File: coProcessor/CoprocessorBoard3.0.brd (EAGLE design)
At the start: 101.6 x 101.6 mm, 76 parts, among them IC1 STM32F405RGT6

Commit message: (Hulk) Smash
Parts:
- added C1: (no value), rcl:E2-5
- moved GPIO_CONNECTOR 17.9 mm to (43.5, 26.1)
- moved OSC_C1 3.70 mm to (43.7, 37.0)
- moved DEBUG 3.38 mm to (31.5, 34.5), turned to 90 degrees
- moved OSC_C2 3.31 mm to (48.3, 37.1)
- moved OSCILLATOR 2.84 mm to (47.2, 33.0)
- moved POWER_JACK 1.42 mm to (5.16, 17.4)
- moved D+SERIES 0.63 mm to (33.3, 74.9)
- moved D-SERIES 0.61 mm to (36.2, 74.9)
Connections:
- net 3V3: now also C1.+
- net GND: now also C1.-
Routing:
- net PC14: track 8.27 -> 29.1 mm
- net 3V3: track 266.0 -> 286.4 mm
- net PC13: track 8.81 -> 27.9 mm
- net MISSION_START: track 58.7 -> 77.5 mm
- net SWITCH_3: track 59.7 -> 77.4 mm
- net SWITCH_4: track 60.3 -> 77.5 mm
- net SWITCH_5: track 61.2 -> 78.0 mm
- net PB8: track 15.6 -> 30.9 mm
- net GND: track 82.7 -> 89.1 mm, vias 13 -> 14
- net RCC_OSC_OUT: track 17.8 -> 19.6 mm
- net USB_OTG_HS_DM: track 10.6 -> 11.2 mm
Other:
- board text added: "3.3V"
- board text added: "JTDI"
- board text added: "PA4"
- board text added: "PA5"
- board text added: "PC4"
- board text added: "PC5"
- board text added: "PC6"
- board text added: "PC7"
- board text added: "SWDIO"

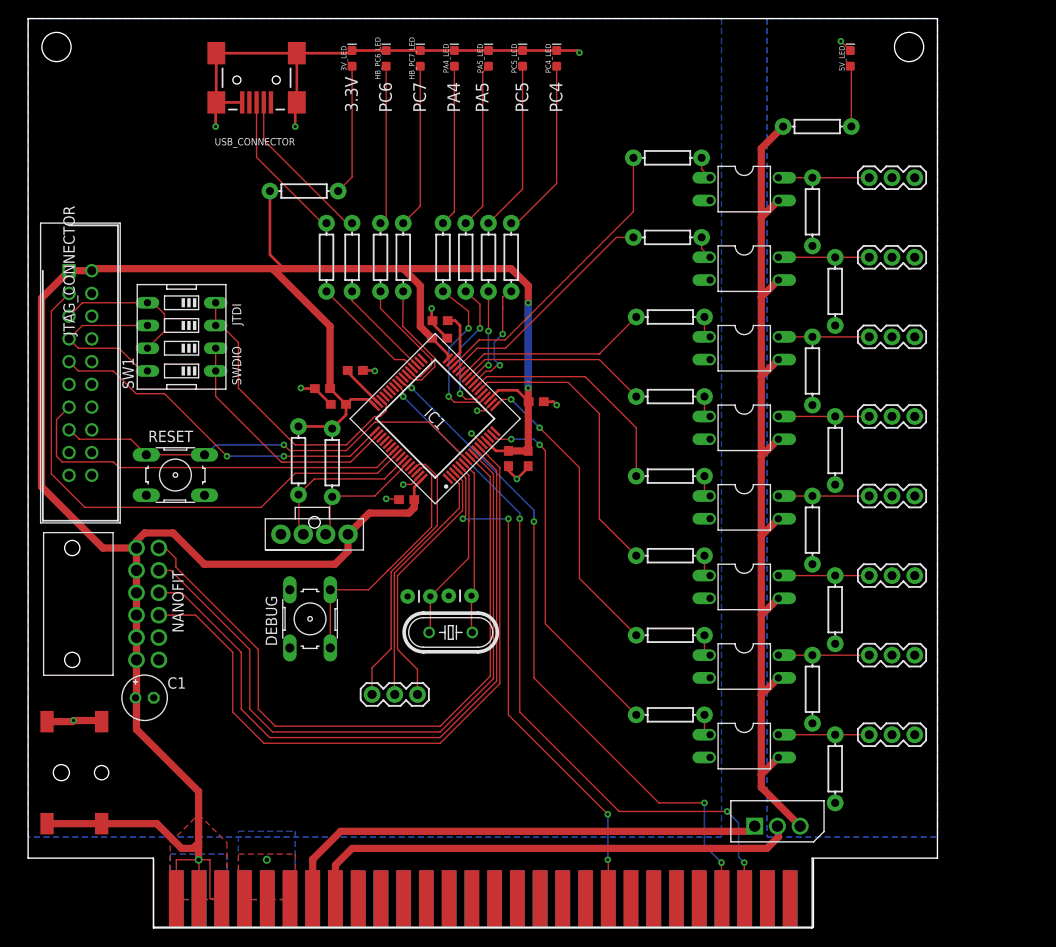
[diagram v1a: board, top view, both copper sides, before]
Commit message: Adding labels to everything
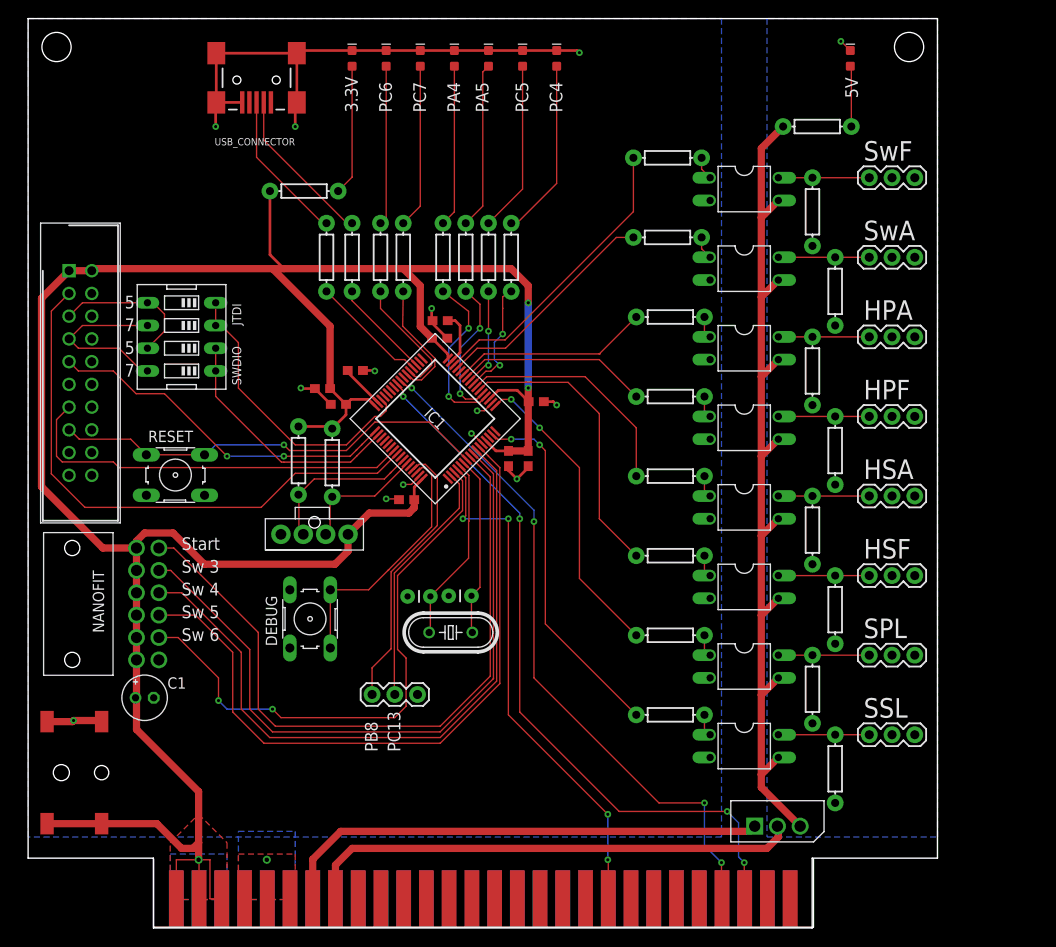
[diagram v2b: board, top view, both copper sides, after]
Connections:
- removed net PC14: GPIO_CONNECTOR.1, IC1.3
- new net SWITCH_6: IC1.3, SWITCH_CONNECTOR.CK2
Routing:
- net SWITCH_6: track 0.00 -> 63.3 mm, vias 0 -> 2
- net PC14: track 29.1 -> 0.00 mm
- net MISSION_START: track 77.5 -> 78.8 mm
- net RCC_OSC_OUT: track 19.6 -> 20.1 mm
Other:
- board text added: "5"
- board text added: "5V"
- board text added: "7"
- board text added: "HPA"
- board text added: "HPF"
- board text added: "HSA"
- board text added: "HSF"
- board text added: "PB8"
- board text added: "PC13"
- board text added: "SPL"
- board text added: "SSL"
- board text added: "Start"
- board text added: "Sw 3"
- board text added: "Sw 4"
- board text added: "Sw 5"
- board text added: "Sw 6"
- board text added: "SwA"
- board text added: "SwF"

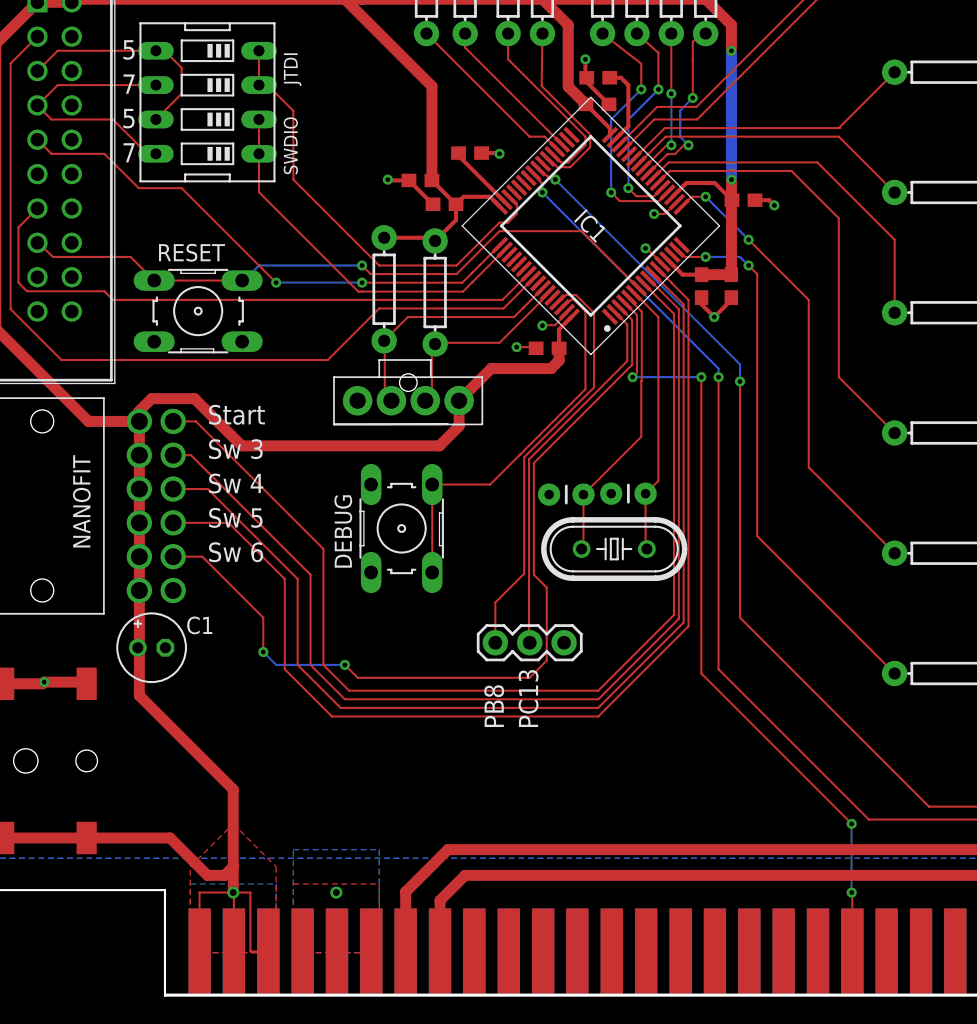
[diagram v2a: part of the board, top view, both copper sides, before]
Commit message: Added low pass filter, ran DRC fixed weird issue
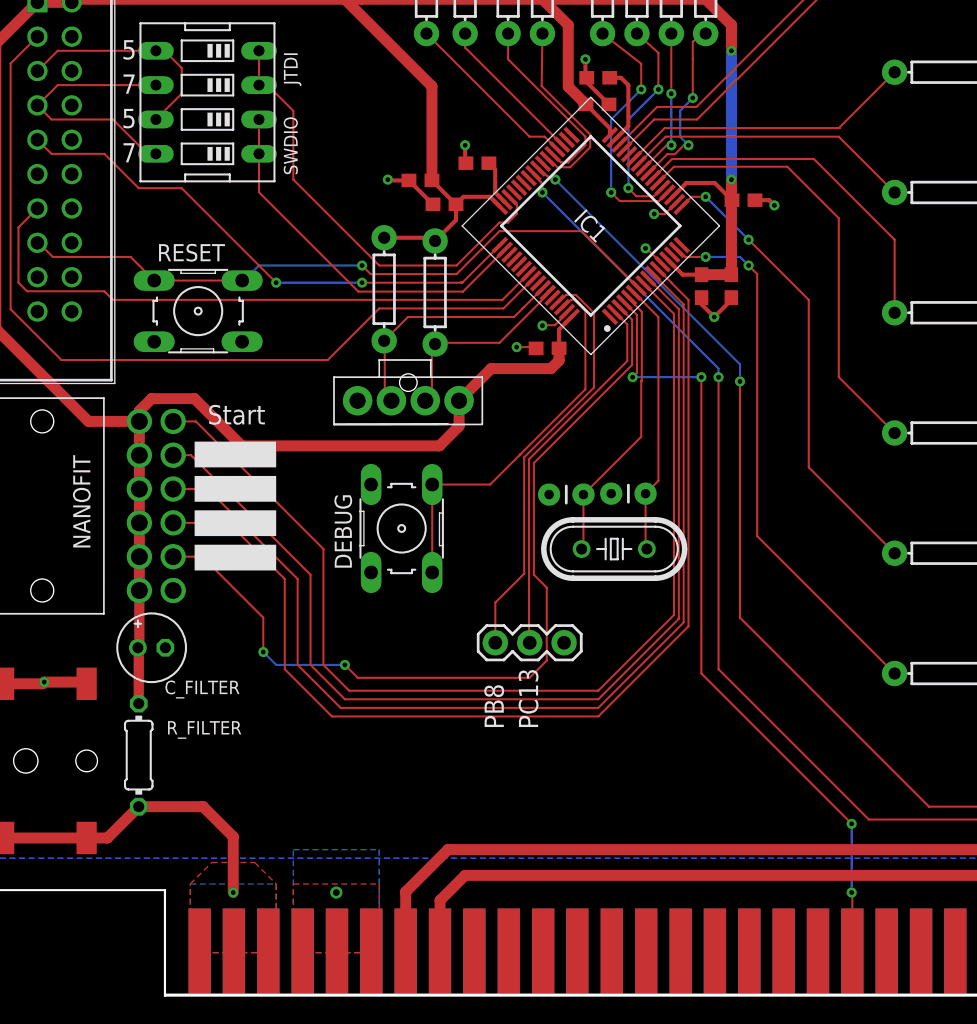
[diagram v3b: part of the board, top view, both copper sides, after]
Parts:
- added R_FILTER: (no value), rcl:0204/7
- moved CAP2 0.92 mm to (37.1, 61.5), turned to 180 degrees
- renumbered C1 to C_FILTER
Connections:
- new net 3V3_RAW: POWER_JACK.1.1, POWER_JACK.1.2, R_FILTER.1, U$1.3.3VP1, U$1.3.3VP2, U$1.3.3VP3, U$1.3.3V_4, U$1.3.3V_5, U$1.3.3V_6
- net 3V3: now also R_FILTER.2; no longer POWER_JACK.1.1, POWER_JACK.1.2, U$1.3.3VP1, U$1.3.3VP2, U$1.3.3VP3, U$1.3.3V_4, U$1.3.3V_5, U$1.3.3V_6
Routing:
- net 3V3: track 286.4 -> 233.0 mm, vias 3 -> 2
- net 3V3_RAW: track 0.00 -> 22.9 mm, vias 0 -> 1
- net VCAP2: track 5.03 -> 3.36 mm
- added copper zone on layer 1, net 3V3_RAW
- added copper zone on layer 16, net 3V3_RAW
- removed copper zone on layer 1, net 3V3
- removed copper zone on layer 16, net 3V3
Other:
- board text removed: "Sw 3"
- board text removed: "Sw 4"
- board text removed: "Sw 5"
- board text removed: "Sw 6"

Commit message: Merging to fix with the stuff
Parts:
- added ESC_CONNECTOR_1: 455-1750-1-ND, SparkFun-Connectors:1X03
- added OPTOCOUPLER_1: SFH610, optocoupler:DIL04
- added O_IN_1: 220, SparkFun-Resistors:AXIAL-0.3
- added O_R1: 10k, SparkFun-Resistors:AXIAL-0.3
- moved O_IN_2 9.23 mm to (65.7, 30.8)
- moved O_R2 7.31 mm to (90.5, 25.1)
- moved OPTOCOUPLER_2 7.23 mm to (80.0, 27.5)
- moved ESC_CONNECTOR_2 7.20 mm to (94.0, 28.8)
- moved O_IN_4 7.16 mm to (69.5, 39.5)
- moved OPTOCOUPLER_4 6.52 mm to (80.0, 35.7)
- moved ESC_CONNECTOR_4 6.49 mm to (94.0, 37.0)
- moved O_IN_5 6.49 mm to (69.5, 47.7)
- moved O_R4 6.30 mm to (87.6, 33.0)
- moved O_IN_6 5.83 mm to (69.5, 55.9)
- moved OPTOCOUPLER_5 5.80 mm to (80.0, 43.9)
- moved ESC_CONNECTOR_5 5.78 mm to (94.0, 45.1)
- moved O_R5 5.71 mm to (90.2, 41.3)
- moved O_R6 5.19 mm to (87.6, 49.6)
- moved O_IN_7 5.18 mm to (69.5, 64.0)
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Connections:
- new net N$1: ESC_CONNECTOR_1.1, OPTOCOUPLER_1.4, O_R1.P$1
- new net N$3: OPTOCOUPLER_1.1, O_IN_1.P$2
- net +5V: now also OPTOCOUPLER_1.3
- net GND: now also OPTOCOUPLER_1.2
- net GNDBAT: now also ESC_CONNECTOR_1.3, O_R1.P$2
- net SURGEPORTHI: now also O_IN_1.P$1
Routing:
- net SURGEPORTHI: track 0.00 -> 40.7 mm, vias 0 -> 2
- net N$1: track 0.00 -> 19.0 mm
- net SURGESTBDLOW: track 40.4 -> 30.9 mm
- net SURGEPORTLOW: track 34.2 -> 26.5 mm
- net HEAVE_STBD_AFT: track 26.4 -> 18.7 mm
- net HEAVE_STBD_FWD: track 33.0 -> 26.0 mm
- net 3V3_RAW: track 22.9 -> 28.8 mm
- net N$21: track 2.49 -> 7.49 mm
- net SW_FWD: track 33.3 -> 37.6 mm
- net N$3: track 0.00 -> 3.90 mm
- net SW_AFT: track 25.7 -> 29.3 mm
- net N$42: track 6.79 -> 3.29 mm
- net HEAVE_PORT_FWD: track 21.5 -> 18.5 mm
- net SDA_BKPLN: track 76.0 -> 78.6 mm
- net +5V: track 102.5 -> 104.9 mm
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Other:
- board text added: "Spare"
- board text added: "The Ohio State Univeristy Center For Automotive Research Underwater Robotics Team CoProcessor Board -- Rev. 3.0"
